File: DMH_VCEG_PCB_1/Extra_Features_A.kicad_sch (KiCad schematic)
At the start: 51 parts, among them J22 Conn_01x10_PinHeader, J23 Conn_01x10_PinHeader, Q4 BC548, SW1 SW_DPDT_x2, SW3 SW_SPDT_321_OnOff, SW4 SW_DPDT_x2_On-Off-(On), U1 TL074, U19 4001, U3 40106, U8 TL074

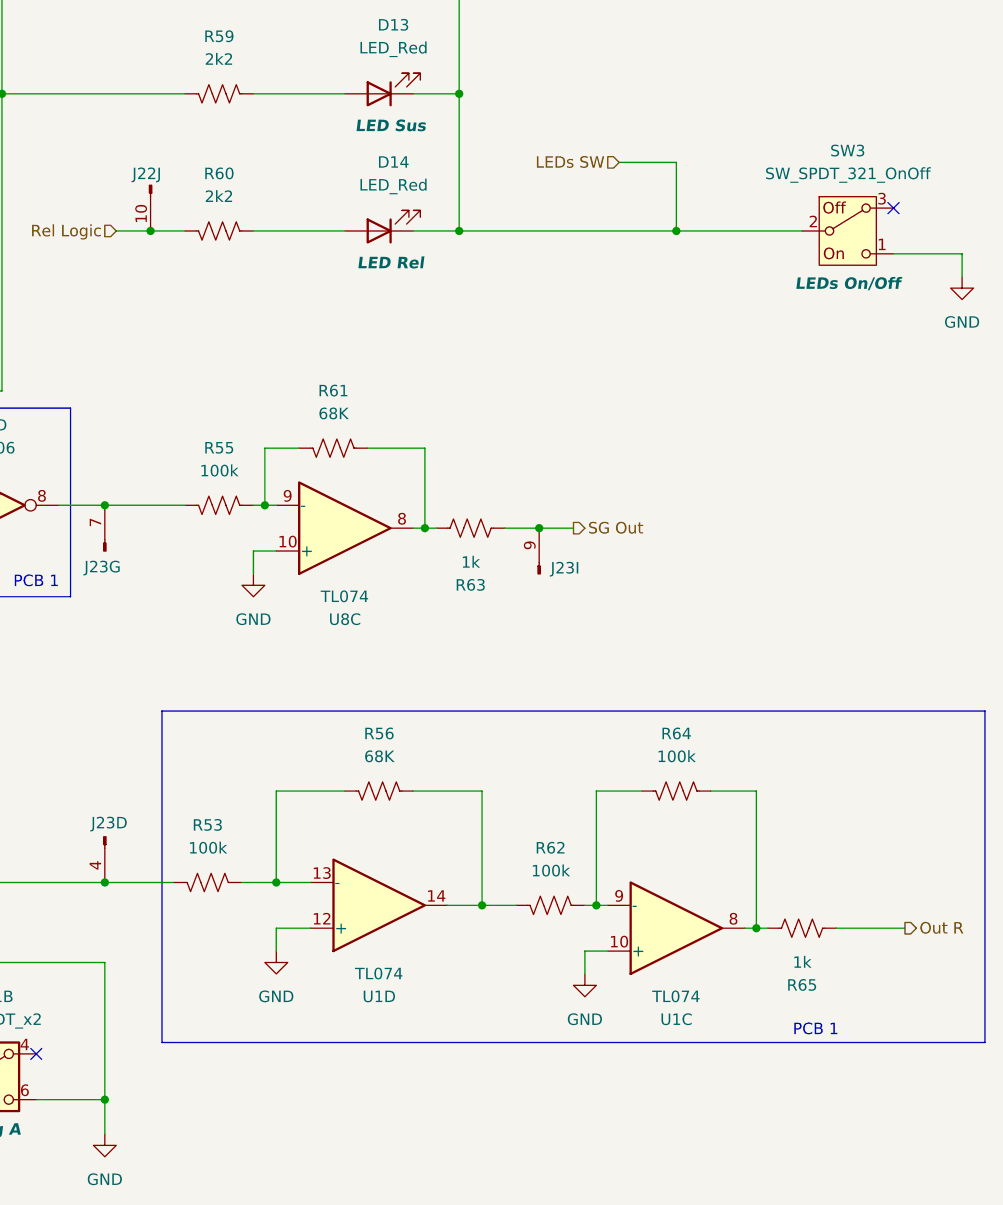
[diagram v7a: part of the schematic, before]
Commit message: Added Output attenuation circuit
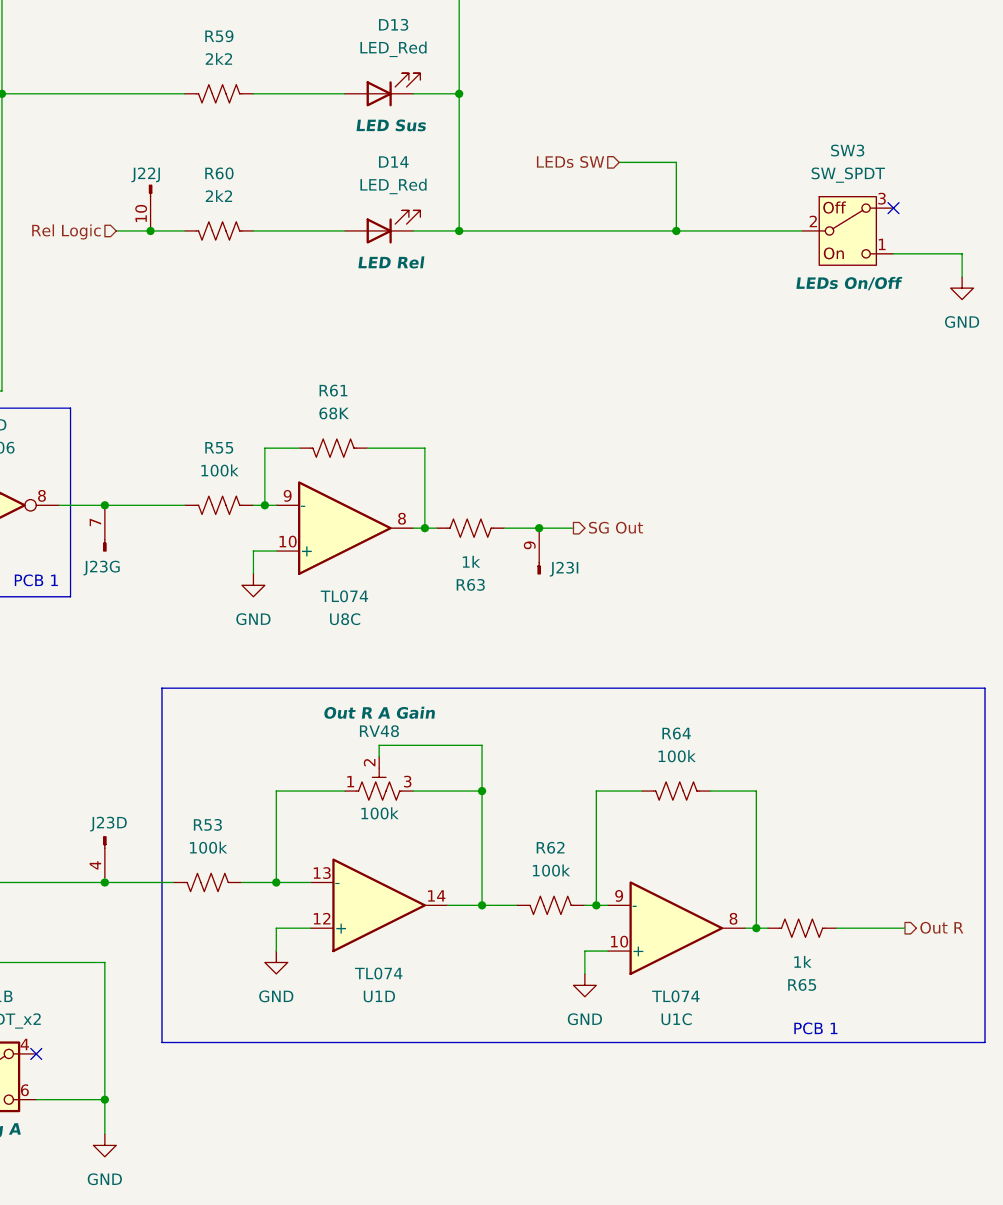
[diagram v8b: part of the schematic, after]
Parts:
- removed R56: 68K, Resistor_THT:R_Axial_DIN0207_L6.3mm_D2.5mm_P7.62mm_Horizontal, symbol Device:R_US
- added RV48: 100k, Potentiometer_THT:Potentiometer_Bourns_3296X_Horizontal, symbol Device:R_Potentiometer_Trim_US
- SW3: value SW_SPDT_321_OnOff -> SW_SPDT
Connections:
- net at R53.2, U1.13 (-): now also RV48.1
- net at R62.1, U1.14: now also RV48.2, RV48.3
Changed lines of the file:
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@@
 	)
 	(rectangle
-		(start 165.1 124.46)
+		(start 165.1 121.92)
 		(end 256.54 161.29)
 		(stroke
@@
 	)
 	(junction
+		(at 200.66 133.35)
+		(diameter 0)
+		(color 0 0 0 0)
+	)
+	(junction
 		(at 88.9 72.39)
 		(diameter 0)
@@
 	(wire
 		(pts
+			(xy 189.23 129.54) (xy 189.23 128.27)
+		)
+		(stroke
+			(width 0)
+			(type default)
+		)
+	)
+	(wire
+		(pts
 			(xy 176.53 101.6) (xy 177.8 101.6)
 		)
@@
 	(wire
 		(pts
+			(xy 189.23 128.27) (xy 200.66 128.27)
+		)
+		(stroke
+			(width 0)
+			(type default)
+		)
+	)
+	(wire
+		(pts
 			(xy 33.02 152.4) (xy 38.1 152.4)
 		)
@@
 	(wire
 		(pts
+			(xy 200.66 128.27) (xy 200.66 133.35)
+		)
+		(stroke
+			(width 0)
+			(type default)
+		)
+	)
+	(wire
+		(pts
 			(xy 109.22 83.82) (xy 109.22 99.06)
 		)
@@
 			)
 		)
-		(property "Value" "SW_SPDT_321_OnOff"
+		(property "Value" "SW_SPDT"
 			(at 241.3 64.77 0)
 			(effects
@@
 	)
 	(symbol
+		(lib_id "Device:R_Potentiometer_Trim_US")
+		(at 189.23 133.35 90)
+		(unit 1)
+		(exclude_from_sim no)
+		(in_bom yes)
+		(on_board yes)
+		(dnp no)
+		(property "Reference" "RV48"
+			(at 189.23 126.746 90)
+			(effects
+				(font
+					(size 1.27 1.27)
+				)
+			)
+		)
+		(property "Value" "100k"
+			(at 189.23 135.89 90)
+			(effects
+				(font
+					(size 1.27 1.27)
+				)
+			)
+		)
+		(property "Footprint" "Potentiometer_THT:Potentiometer_Bourns_3296X_Horizontal"
+			(at 189.23 133.35 0)
+			(effects
+				(font
+					(size 1.27 1.27)
+				)
+				(hide yes)
+			)
+		)
+		(property "Datasheet" "~"
+			(at 189.23 133.35 0)
+			(effects
+				(font
+					(size 1.27 1.27)
+				)
+				(hide yes)
+			)
+		)
+		(property "Description" "Trim-potentiometer, US symbol"
+			(at 189.23 133.35 0)
+			(effects
+				(font
+					(size 1.27 1.27)
+				)
+				(hide yes)
+			)
+		)
+		(property "Function" "Out R A Gain"
+			(at 189.23 124.714 90)
+			(effects
+				(font
+					(size 1.27 1.27)
+					(thickness 0.254)
+					(bold yes)
+					(italic yes)
+				)
+			)
+		)
+		(pin "2"
+		)
+		(pin "1"
+		)
+		(pin "3"
+		)
+		(instances
+			(project "DMH_VCEG_PCB_1"
+				(path "/58f4306d-5387-4983-bb08-41a2313fd315/dfc6a801-157b-43f6-bf92-8048d56e52a2"
+					(reference "RV48")
+					(unit 1)
+				)
+			)
+		)
+	)
+	(symbol
 		(lib_id "power:+12V")
 		(at 82.55 113.03 0)
@@
 				)
 			)
-		)
-	)
-	(symbol
-		(lib_id "Device:R_US")
-		(at 189.23 133.35 90)
-		(mirror x)
-		(unit 1)
-		(exclude_from_sim no)
-		(in_bom yes)
-		(on_board yes)
-		(dnp no)
-		(property "Reference" "R56"
-			(at 189.23 127 90)
-			(effects
-				(font
-					(size 1.27 1.27)
-				)
-			)
-		)
-		(property "Value" "68K"
-			(at 189.23 129.54 90)
-			(effects
-				(font
-					(size 1.27 1.27)
-				)
-			)
-		)
-		(property "Footprint" "Resistor_THT:R_Axial_DIN0207_L6.3mm_D2.5mm_P7.62mm_Horizontal"
-			(at 189.484 134.366 90)
-			(effects
-				(font
-					(size 1.27 1.27)
-				)
-				(hide yes)
-			)
-		)
-		(property "Datasheet" "~"
-			(at 189.23 133.35 0)
-			(effects
-				(font
-					(size 1.27 1.27)
-				)
-				(hide yes)
-			)
-		)
-		(property "Description" "Resistor, US symbol"
-			(at 189.23 133.35 0)
-			(effects
-				(font
-					(size 1.27 1.27)
-				)
-				(hide yes)
-			)
-		)
-		(pin "2"
-		)
-		(pin "1"
-		)
-		(instances
-			(project "DMH_VCEG_PCB_1"
-				(path "/58f4306d-5387-4983-bb08-41a2313fd315/dfc6a801-157b-43f6-bf92-8048d56e52a2"
-					(reference "R56")
-					(unit 1)
-				)
-			)
